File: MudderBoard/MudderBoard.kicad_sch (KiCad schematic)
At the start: 0 parts

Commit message: Iceberg Logo
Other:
- note removed: "PENIS"
- company: Iceberg ASV -> (none)

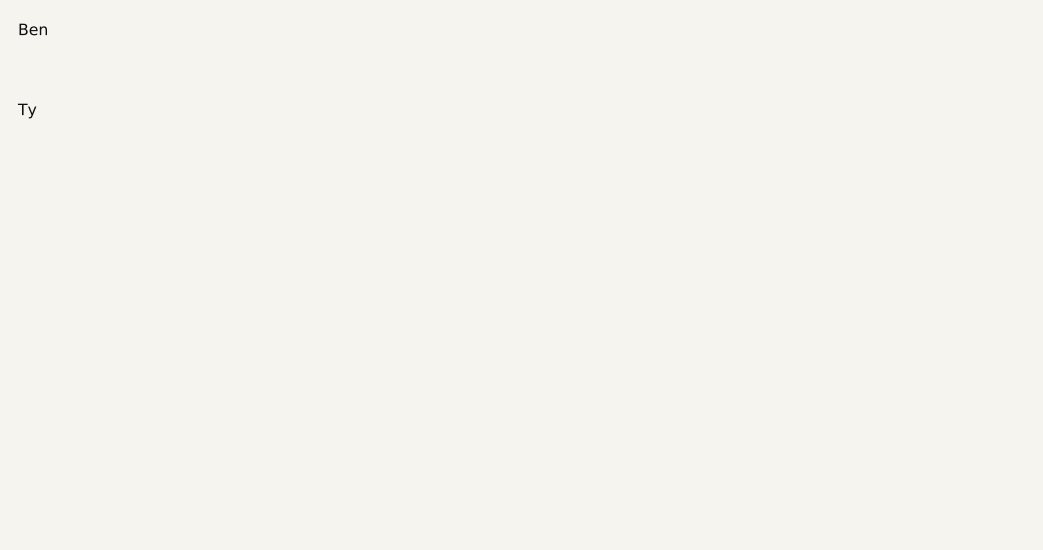
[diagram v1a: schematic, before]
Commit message: LiDar Schematic
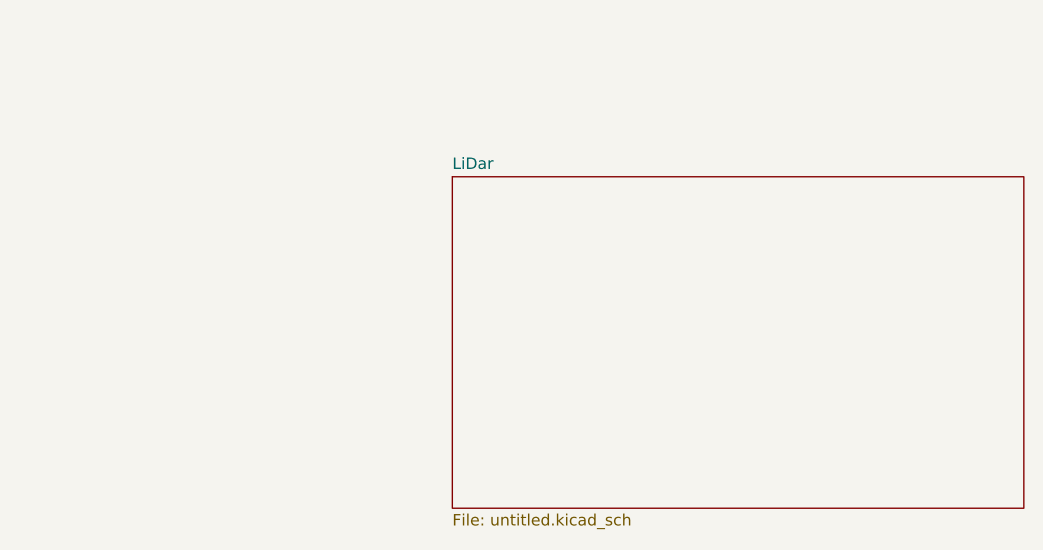
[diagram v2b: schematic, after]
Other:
- added sheet LiDar (untitled.kicad_sch)
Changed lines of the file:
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@@
 		)
 	)
-	(label "Ben"
-		(at 20.32 24.13 0)
+	(sheet
+		(at 68.58 39.37)
+		(size 63.5 36.83)
 		(fields_autoplaced yes)
-		(effects
-			(font
-				(size 1.27 1.27)
+		(stroke
+			(width 0.1524)
+			(type solid)
+		)
+		(fill
+			(color 0 0 0 0.0000)
+		)
+		(property "Sheetname" "LiDar"
+			(at 68.58 38.6584 0)
+			(effects
+				(font
+					(size 1.27 1.27)
+				)
+				(justify left bottom)
 			)
-			(justify left bottom)
+		)
+		(property "Sheetfile" "untitled.kicad_sch"
+			(at 68.58 76.7846 0)
+			(effects
+				(font
+					(size 1.27 1.27)
+				)
+				(justify left top)
+			)
+		)
+		(instances
+			(project "MudderBoard"
+				(path "/cdf98bf7-80ce-4b13-b655-e6c7c589c122"
+					(page "2")
+				)
+			)
 		)
 	)
-	(label "Ty"
-		(at 20.32 33.02 0)
-		(fields_autoplaced yes)
-		(effects
-			(font
-				(size 1.27 1.27)
-			)
-			(justify left bottom)
-		)
-	)

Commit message: Block Diagram
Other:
- added sheet Battery Monitor (battmon.kicad_sch)
- added sheet ESC (ESC.kicad_sch)
- added sheet Jetson (jetson.kicad_sch)
- added sheet PWM-DC (pwm-dc.kicad_sch)
- added sheet Pixhawk (pixhawk.kicad_sch)
- added sheet Wifi Bullet (wifibullet.kicad_sch)
- sheet LiDar: file untitled.kicad_sch -> lidar.kicad_sch
- note added: "Schematic:"

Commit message: post meeting
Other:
- added sheet Untitled Sheet (untitled.kicad_sch)
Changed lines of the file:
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@@
+	)
+	(sheet
+		(at 29.21 157.48)
+		(size 40.64 17.78)
+		(fields_autoplaced yes)
+		(stroke
+			(width 0.1524)
+			(type solid)
+		)
+		(fill
+			(color 0 0 0 0.0000)
+		)
+		(property "Sheetname" "Untitled Sheet"
+			(at 29.21 156.7684 0)
+			(effects
+				(font
+					(size 1.27 1.27)
+				)
+				(justify left bottom)
+			)
+		)
+		(property "Sheetfile" "untitled.kicad_sch"
+			(at 29.21 175.8446 0)
+			(effects
+				(font
+					(size 1.27 1.27)
+				)
+				(justify left top)
+			)
+		)
+		(instances
+			(project "MudderBoard"
+				(path "/cdf98bf7-80ce-4b13-b655-e6c7c589c122"
+					(page "9")
+				)
+			)
+		)
 	)
 	(sheet

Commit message: Component Sorting
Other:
- removed sheet Untitled Sheet
- note added: "PWM_CH2"
- note added: "PWM_CH3"
- note added: "PWM_CH5"
- note added: "VCC"
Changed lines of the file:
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@@
+		)
+	)
+	(text "VCC"
+		(exclude_from_sim no)
+		(at 115.57 63.246 0)
+		(effects
+			(font
+				(size 2.54 2.54)
+				(bold yes)
+				(color 255 0 0 1)
+			)
+		)
+	)
+	(text "PWM_CH3"
+		(exclude_from_sim no)
+		(at 86.106 27.686 0)
+		(effects
+			(font
+				(size 2.54 2.54)
+				(bold yes)
+				(color 0 0 255 1)
+			)
+		)
+	)
+	(text "VCC"
+		(exclude_from_sim no)
+		(at 115.316 77.47 0)
+		(effects
+			(font
+				(size 2.54 2.54)
+				(bold yes)
+				(color 255 0 0 1)
+			)
+		)
+	)
+	(text "VCC"
+		(exclude_from_sim no)
+		(at 110.998 113.792 0)
+		(effects
+			(font
+				(size 2.54 2.54)
+				(bold yes)
+				(color 255 0 0 1)
+			)
+		)
+	)
+	(text "VCC"
+		(exclude_from_sim no)
+		(at 92.456 149.352 0)
+		(effects
+			(font
+				(size 2.54 2.54)
+				(bold yes)
+				(color 255 0 0 1)
+			)
+		)
+	)
+	(text "PWM_CH2"
+		(exclude_from_sim no)
+		(at 86.868 17.018 0)
+		(effects
+			(font
+				(size 2.54 2.54)
+				(bold yes)
+				(color 0 0 255 1)
+			)
+		)
+	)
+	(text "PWM_CH5"
+		(exclude_from_sim no)
+		(at 85.344 56.896 0)
+		(effects
+			(font
+				(size 2.54 2.54)
+				(bold yes)
+				(color 0 0 255 1)
+			)
+		)
+	)
+	(text "VCC"
+		(exclude_from_sim no)
+		(at 115.57 97.282 0)
+		(effects
+			(font
+				(size 2.54 2.54)
+				(bold yes)
+				(color 255 0 0 1)
+			)
 		)
 	)
@@
 				(size 4.445 4.445)
 				(bold yes)
+			)
+		)
+	)
+	(text "VCC"
+		(exclude_from_sim no)
+		(at 113.538 41.656 0)
+		(effects
+			(font
+				(size 2.54 2.54)
+				(bold yes)
+				(color 255 0 0 1)
+			)
+		)
+	)
+	(text "VCC"
+		(exclude_from_sim no)
+		(at 96.774 133.096 0)
+		(effects
+			(font
+				(size 2.54 2.54)
+				(bold yes)
+				(color 255 0 0 1)
 			)
 		)
@@
 				)
 			)
-		)
-	)
-	(sheet
-		(at 29.21 157.48)
-		(size 40.64 17.78)
-		(fields_autoplaced yes)
-		(stroke
-			(width 0.1524)
-			(type solid)
-		)
-		(fill
-			(color 0 0 0 0.0000)
-		)
-		(property "Sheetname" "Untitled Sheet"
-			(at 29.21 156.7684 0)
-			(effects
-				(font
-					(size 1.27 1.27)
-				)
-				(justify left bottom)
-			)
-		)
-		(property "Sheetfile" "untitled.kicad_sch"
-			(at 29.21 175.8446 0)
-			(effects
-				(font
-					(size 1.27 1.27)
-				)
-				(justify left top)
-			)
-		)
-		(instances
-			(project "MudderBoard"
-				(path "/cdf98bf7-80ce-4b13-b655-e6c7c589c122"
-					(page "9")
-				)
-			)

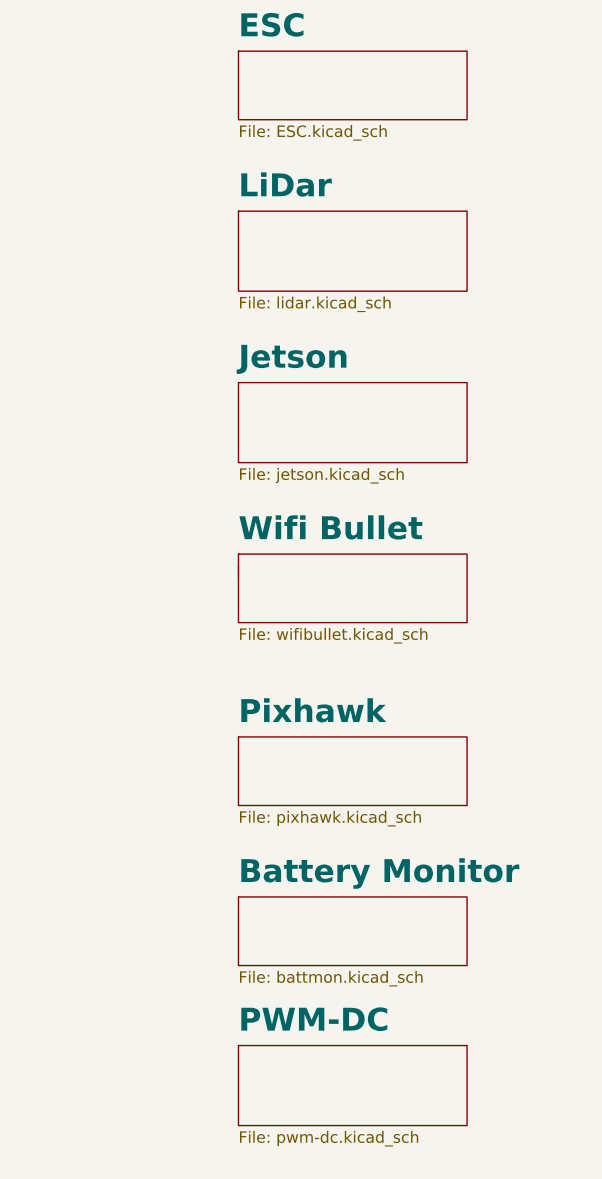
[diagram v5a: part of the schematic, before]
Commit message: mosfet selection LiDar
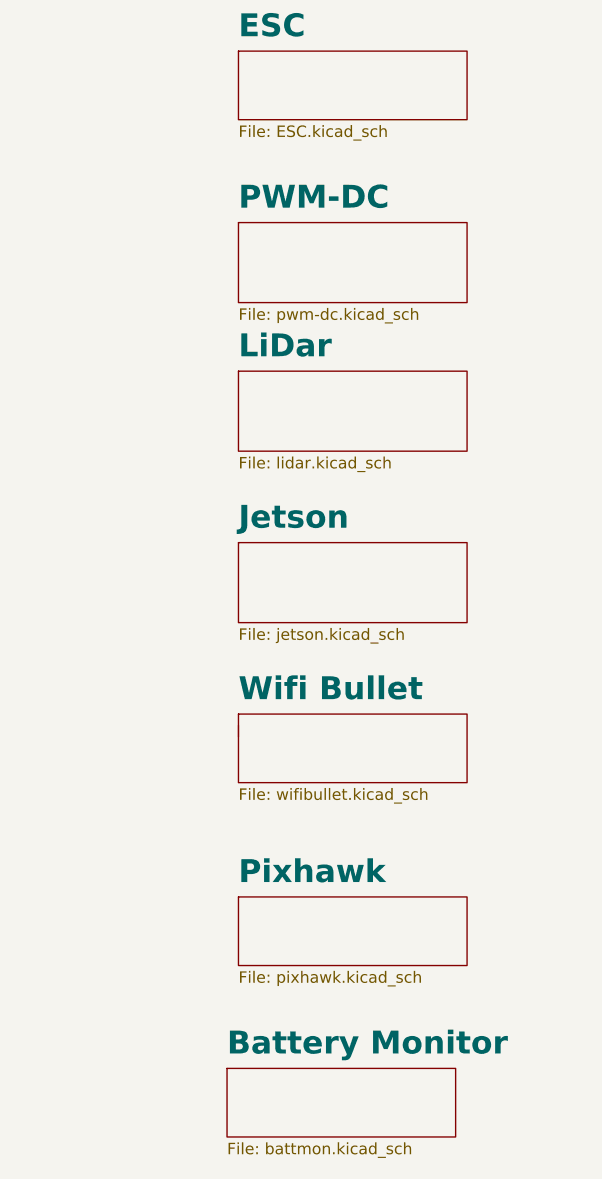
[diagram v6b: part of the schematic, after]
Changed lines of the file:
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@@
 	(polyline
 		(pts
-			(xy 234.95 93.98) (xy 234.95 95.25)
+			(xy 234.95 111.76) (xy 234.95 113.03)
 		)
 		(stroke
@@
 	)
 	(sheet
-		(at 234.95 113.03)
+		(at 234.95 130.81)
 		(size 25.4 7.62)
 		(fields_autoplaced yes)
@@
 		)
 		(property "Sheetname" "Pixhawk"
-			(at 234.95 111.6834 0)
+			(at 234.95 129.4634 0)
 			(effects
 				(font
@@
 		)
 		(property "Sheetfile" "pixhawk.kicad_sch"
-			(at 234.95 121.2346 0)
+			(at 234.95 139.0146 0)
 			(effects
 				(font
@@
 	)
 	(sheet
-		(at 234.95 147.32)
+		(at 234.95 55.88)
 		(size 25.4 8.89)
 		(fields_autoplaced yes)
@@
 		)
 		(property "Sheetname" "PWM-DC"
-			(at 234.95 145.9734 0)
+			(at 234.95 54.5334 0)
 			(effects
 				(font
@@
 		)
 		(property "Sheetfile" "pwm-dc.kicad_sch"
-			(at 234.95 156.7946 0)
+			(at 234.95 65.3546 0)
 			(effects
 				(font
@@
 	)
 	(sheet
-		(at 234.95 92.71)
+		(at 234.95 110.49)
 		(size 25.4 7.62)
 		(fields_autoplaced yes)
@@
 		)
 		(property "Sheetname" "Wifi Bullet"
-			(at 234.95 91.3634 0)
+			(at 234.95 109.1434 0)
 			(effects
 				(font
@@
 		)
 		(property "Sheetfile" "wifibullet.kicad_sch"
-			(at 234.95 100.9146 0)
+			(at 234.95 118.6946 0)
 			(effects
 				(font
@@
 	)
 	(sheet
-		(at 234.95 73.66)
+		(at 234.95 91.44)
 		(size 25.4 8.89)
 		(fields_autoplaced yes)
@@
 		)
 		(property "Sheetname" "Jetson"
-			(at 234.95 72.3134 0)
+			(at 234.95 90.0934 0)
 			(effects
 				(font
@@
 		)
 		(property "Sheetfile" "jetson.kicad_sch"
-			(at 234.95 83.1346 0)
+			(at 234.95 100.9146 0)
 			(effects
 				(font
@@
 	)
 	(sheet
-		(at 234.95 54.61)
+		(at 234.95 72.39)
 		(size 25.4 8.89)
 		(fields_autoplaced yes)
@@
 		)
 		(property "Sheetname" "LiDar"
-			(at 234.95 53.2634 0)
+			(at 234.95 71.0434 0)
 			(effects
 				(font
@@
 		)
 		(property "Sheetfile" "lidar.kicad_sch"
-			(at 234.95 64.0846 0)
+			(at 234.95 81.8646 0)
 			(effects
 				(font
@@
 	)
 	(sheet
-		(at 234.95 130.81)
+		(at 233.68 149.86)
 		(size 25.4 7.62)
 		(fields_autoplaced yes)
@@
 		)
 		(property "Sheetname" "Battery Monitor"
-			(at 234.95 129.4634 0)
+			(at 233.68 148.5134 0)
 			(effects
 				(font
@@
 		)
 		(property "Sheetfile" "battmon.kicad_sch"
-			(at 234.95 139.0146 0)
+			(at 233.68 158.0646 0)
 			(effects
 				(font

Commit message: deleted BattMon
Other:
- removed sheet Battery Monitor
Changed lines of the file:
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@@
 	(polyline
 		(pts
-			(xy 83.82 151.13) (xy 127 151.13)
-		)
-		(stroke
-			(width 0)
-			(type default)
-			(color 255 0 0 1)
-		)
-	)
-	(polyline
-		(pts
 			(xy 109.22 64.77) (xy 144.78 64.77)
 		)
@@
 	(polyline
 		(pts
-			(xy 127 151.13) (xy 144.78 151.13)
-		)
-		(stroke
-			(width 0)
-			(type default)
-			(color 255 0 0 1)
-		)
-	)
-	(polyline
-		(pts
 			(xy 166.37 19.05) (xy 166.37 36.83)
 		)
@@
 	(polyline
 		(pts
-			(xy 83.82 90.17) (xy 83.82 151.13)
-		)
-		(stroke
-			(width 0)
-			(type default)
-			(color 255 0 0 1)
-		)
-	)
-	(polyline
-		(pts
 			(xy 93.98 87.63) (xy 102.87 87.63)
 		)
@@
 		)
 	)
-	(text_box "Battery Monitor"
-		(exclude_from_sim no)
-		(at 144.78 147.32 0)
-		(size 59.69 12.7)
-		(stroke
-			(width 0)
-			(type default)
-			(color 0 0 255 1)
-		)
-		(fill
-			(type none)
-		)
-		(effects
-			(font
-				(size 4.445 4.445)
-				(bold yes)
-				(color 0 0 255 1)
-			)
-			(justify left top)
-		)
-	)
 	(text_box "ESC (20V)"
 		(exclude_from_sim no)
@@
 		)
 	)
-	(text "VCC"
-		(exclude_from_sim no)
-		(at 92.456 149.352 0)
-		(effects
-			(font
-				(size 2.54 2.54)
-				(bold yes)
-				(color 255 0 0 1)
-			)
-		)
-	)
 	(text "PWM_CH2"
 		(exclude_from_sim no)
@@
 				)
 			)
-		)
-	)
-	(sheet
-		(at 233.68 149.86)
-		(size 25.4 7.62)
-		(fields_autoplaced yes)
-		(stroke
-			(width 0.1524)
-			(type solid)
-		)
-		(fill
-			(color 0 0 0 0.0000)
-		)
-		(property "Sheetname" "Battery Monitor"
-			(at 233.68 148.5134 0)
-			(effects
-				(font
-					(size 2.54 2.54)
-					(bold yes)
-				)
-				(justify left bottom)
-			)
-		)
-		(property "Sheetfile" "battmon.kicad_sch"
-			(at 233.68 158.0646 0)
-			(effects
-				(font
-					(size 1.27 1.27)
-				)
-				(justify left top)
-			)
-		)
-		(instances
-			(project "MudderBoard"
-				(path "/cdf98bf7-80ce-4b13-b655-e6c7c589c122"
-					(page "8")
-				)
-			)

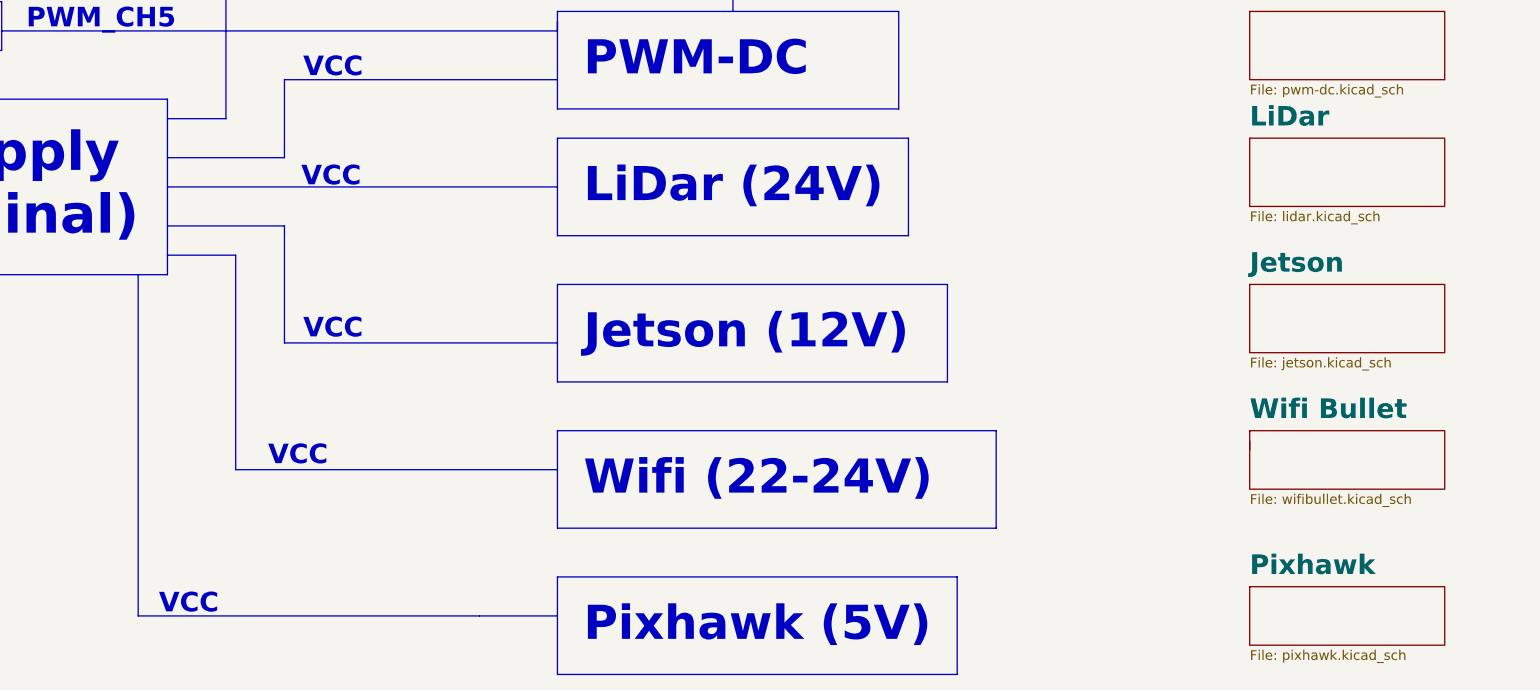
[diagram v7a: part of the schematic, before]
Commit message: Combined Wifi and Lidar Pages
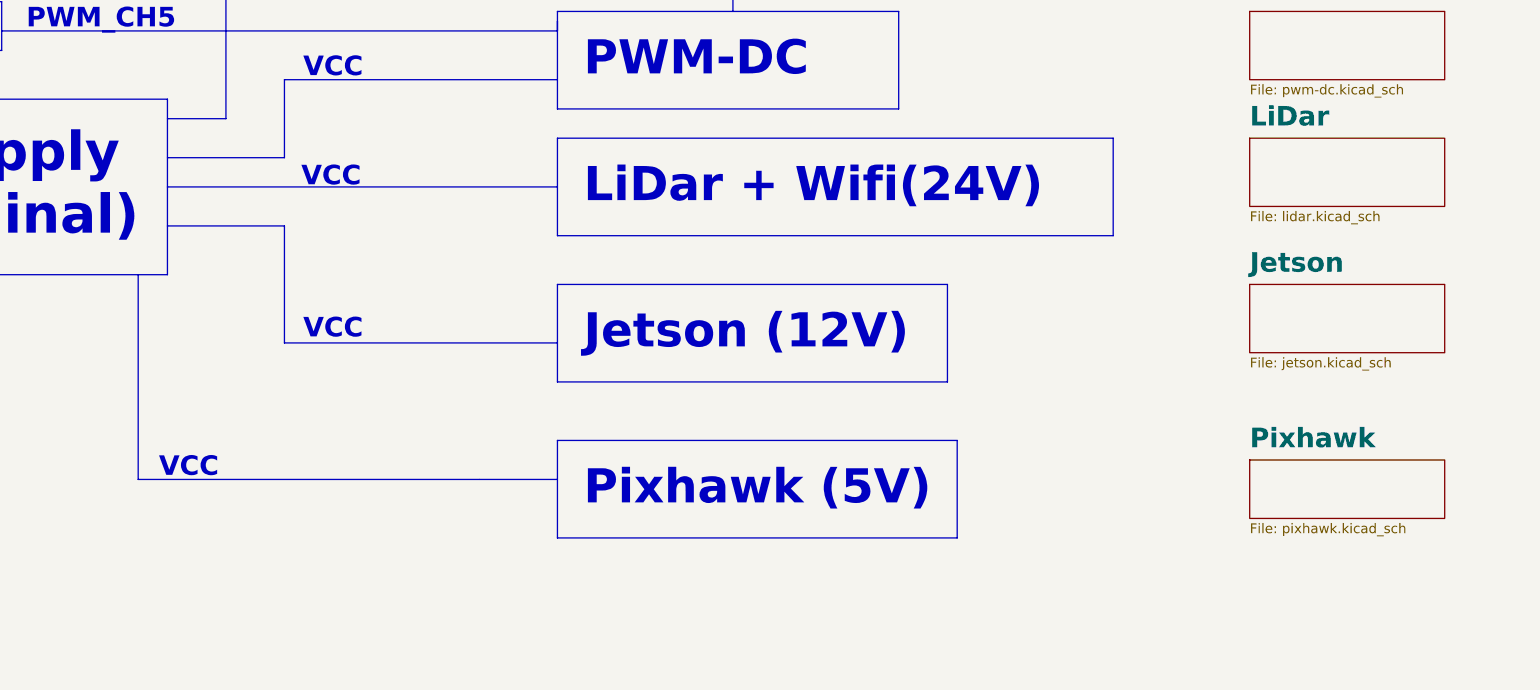
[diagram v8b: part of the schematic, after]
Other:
- removed sheet Wifi Bullet
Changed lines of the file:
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@@
 	(polyline
 		(pts
-			(xy 90.17 90.17) (xy 90.17 134.62)
+			(xy 90.17 90.17) (xy 90.17 116.84)
 		)
 		(stroke
@@
 	(polyline
 		(pts
-			(xy 134.62 134.62) (xy 144.78 134.62)
+			(xy 134.62 116.84) (xy 144.78 116.84)
 		)
 		(stroke
@@
 	(polyline
 		(pts
-			(xy 90.17 134.62) (xy 134.62 134.62)
-		)
-		(stroke
-			(width 0)
-			(type default)
-			(color 255 0 0 1)
-		)
-	)
-	(polyline
-		(pts
-			(xy 234.95 111.76) (xy 234.95 113.03)
-		)
-		(stroke
-			(width 0)
-			(type default)
-		)
-	)
-	(polyline
-		(pts
-			(xy 144.78 115.57) (xy 102.87 115.57)
-		)
-		(stroke
-			(width 0)
-			(type default)
-			(color 255 0 0 1)
-		)
-	)
-	(polyline
-		(pts
-			(xy 102.87 115.57) (xy 102.87 87.63)
+			(xy 90.17 116.84) (xy 134.62 116.84)
 		)
 		(stroke
@@
 	(polyline
 		(pts
-			(xy 93.98 87.63) (xy 102.87 87.63)
-		)
-		(stroke
-			(width 0)
-			(type default)
-			(color 255 0 0 1)
-		)
-	)
-	(polyline
-		(pts
 			(xy 144.78 99.06) (xy 109.22 99.06)
 		)
@@
 	(text_box "Pixhawk (5V)"
 		(exclude_from_sim no)
-		(at 144.78 129.54 0)
+		(at 144.78 111.76 0)
 		(size 52.07 12.7)
 		(stroke
@@
 		)
 	)
-	(text_box "LiDar (24V)"
+	(text_box "LiDar + Wifi(24V)"
 		(exclude_from_sim no)
 		(at 144.78 72.39 0)
-		(size 45.72 12.7)
+		(size 72.39 12.7)
 		(stroke
 			(width 0)
@@
 		)
 	)
-	(text_box "Wifi (22-24V)"
-		(exclude_from_sim no)
-		(at 144.78 110.49 0)
-		(size 57.15 12.7)
-		(stroke
-			(width 0)
-			(type default)
-			(color 255 0 0 1)
-		)
-		(fill
-			(type none)
-		)
-		(effects
-			(font
-				(size 4.445 4.445)
-				(bold yes)
-				(color 255 0 0 1)
-			)
-			(justify left top)
-		)
-	)
 	(text "VCC"
 		(exclude_from_sim no)
@@
 		)
 	)
-	(text "VCC"
-		(exclude_from_sim no)
-		(at 110.998 113.792 0)
-		(effects
-			(font
-				(size 2.54 2.54)
-				(bold yes)
-				(color 255 0 0 1)
-			)
-		)
-	)
 	(text "PWM_CH2"
 		(exclude_from_sim no)
@@
 	(text "VCC"
 		(exclude_from_sim no)
-		(at 96.774 133.096 0)
+		(at 96.774 115.316 0)
 		(effects
 			(font
@@
 	)
 	(sheet
-		(at 234.95 130.81)
+		(at 234.95 114.3)
 		(size 25.4 7.62)
 		(fields_autoplaced yes)
@@
 		)
 		(property "Sheetname" "Pixhawk"
-			(at 234.95 129.4634 0)
+			(at 234.95 112.9534 0)
 			(effects
 				(font
@@
 		)
 		(property "Sheetfile" "pixhawk.kicad_sch"
-			(at 234.95 139.0146 0)
+			(at 234.95 122.5046 0)
 			(effects
 				(font
@@
 			(project "MudderBoard"
 				(path "/cdf98bf7-80ce-4b13-b655-e6c7c589c122"
-					(page "5")
+					(page "4")
 				)
 			)
@@
 			(project "MudderBoard"
 				(path "/cdf98bf7-80ce-4b13-b655-e6c7c589c122"
-					(page "7")
+					(page "6")
 				)
 			)
@@
 			(project "MudderBoard"
 				(path "/cdf98bf7-80ce-4b13-b655-e6c7c589c122"
-					(page "4")
-				)
-			)
-		)
-	)
-	(sheet
-		(at 234.95 110.49)
-		(size 25.4 7.62)
-		(fields_autoplaced yes)
-		(stroke
-			(width 0.1524)
-			(type solid)
-		)
-		(fill
-			(color 0 0 0 0.0000)
-		)
-		(property "Sheetname" "Wifi Bullet"
-			(at 234.95 109.1434 0)
-			(effects
-				(font
-					(size 2.54 2.54)
-					(bold yes)
-				)
-				(justify left bottom)
-			)
-		)
-		(property "Sheetfile" "wifibullet.kicad_sch"
-			(at 234.95 118.6946 0)
-			(effects
-				(font
-					(size 1.27 1.27)
-				)
-				(justify left top)
-			)
-		)
-		(instances
-			(project "MudderBoard"
-				(path "/cdf98bf7-80ce-4b13-b655-e6c7c589c122"
 					(page "3")
 				)
@@
 			(project "MudderBoard"
 				(path "/cdf98bf7-80ce-4b13-b655-e6c7c589c122"
-					(page "6")
+					(page "5")
 				)
 			)
